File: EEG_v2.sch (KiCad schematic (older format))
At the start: 1 part

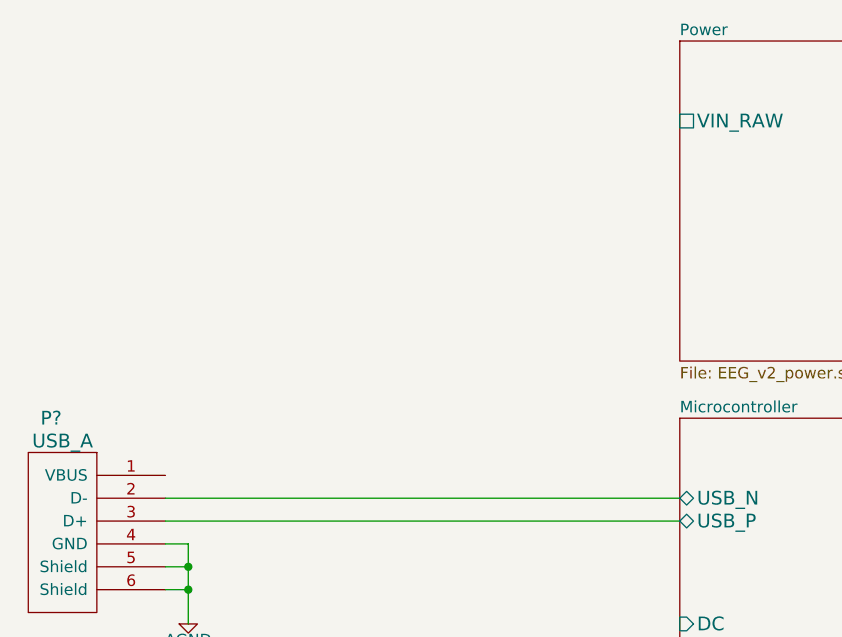
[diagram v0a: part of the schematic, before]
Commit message: Add battery connectors and switch
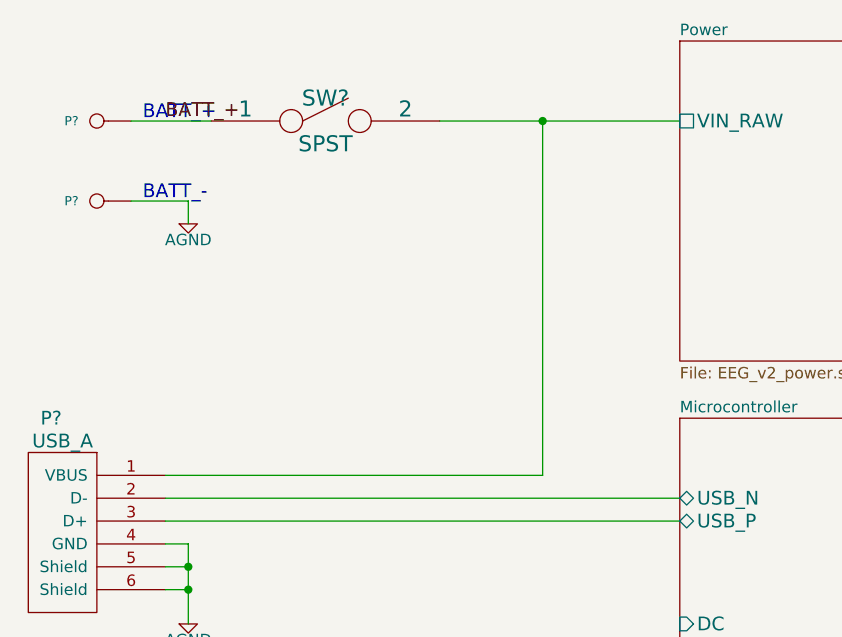
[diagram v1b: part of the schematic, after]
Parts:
- added P? (x2): CONN_1, ~, symbol CONN_1
- added SW?: SPST, ~, symbol SPST
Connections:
- net AGND: now also P?.1
- net Power/VIN_RAW: now also P?.1 (VBUS), SW?.2
- new net BATT_+: P?.1, SW?.1
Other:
- note added: "BATT_+"
- note added: "BATT_-"
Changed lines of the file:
@@
 	1    0    0    -1
 $EndComp
+$Comp
+L SPST SW?
+U 1 1 54C4411E
+P 3350 2900
+F 0 "SW?" H 3350 3000 70  0000 C CNN
+F 1 "SPST" H 3350 2800 70  0000 C CNN
+F 2 "~" H 3350 2900 60  0000 C CNN
+F 3 "~" H 3350 2900 60  0000 C CNN
+	1    3350 2900
+	1    0    0    -1
+$EndComp
+Wire Wire Line
+	3850 2900 4900 2900
+Wire Wire Line
+	2650 4450 4300 4450
+Wire Wire Line
+	4300 4450 4300 2900
+Connection ~ 4300 2900
+$Comp
+L CONN_1 P?
+U 1 1 54C44DCA
+P 2350 2900
+F 0 "P?" H 2430 2900 40  0000 L CNN
+F 1 "CONN_1" H 2350 2955 30  0001 C CNN
+F 2 "~" H 2350 2900 60  0000 C CNN
+F 3 "~" H 2350 2900 60  0000 C CNN
+	1    2350 2900
+	-1   0    0    1
+$EndComp
+$Comp
+L CONN_1 P?
+U 1 1 54C44DD9
+P 2350 3250
+F 0 "P?" H 2430 3250 40  0000 L CNN
+F 1 "CONN_1" H 2350 3305 30  0001 C CNN
+F 2 "~" H 2350 3250 60  0000 C CNN
+F 3 "~" H 2350 3250 60  0000 C CNN
+	1    2350 3250
+	-1   0    0    1
+$EndComp
+Wire Wire Line
+	2500 2900 2850 2900
+Wire Wire Line
+	2500 3250 2750 3250
+Wire Wire Line
+	2750 3250 2750 3350
+$Comp
+L AGND #PWR?
+U 1 1 54C45735
+P 2750 3350
+F 0 "#PWR?" H 2750 3350 40  0001 C CNN
+F 1 "AGND" H 2750 3280 50  0000 C CNN
+F 2 "~" H 2750 3350 60  0000 C CNN
+F 3 "~" H 2750 3350 60  0000 C CNN
+	1    2750 3350
+	1    0    0    -1
+$EndComp
+Text Notes 2550 2900 0    60   ~ 0
+BATT_+
+Text Label 2650 2900 0    60   ~ 0
+BATT_+
+Text Notes 2550 3250 0    60   ~ 0
+BATT_-
 $EndSCHEMATC

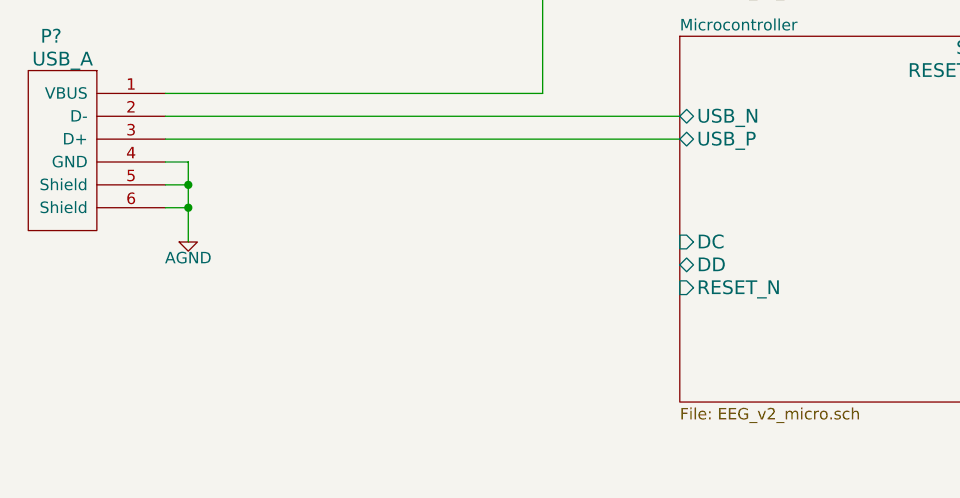
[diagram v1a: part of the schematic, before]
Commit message: Added debug / programming connector
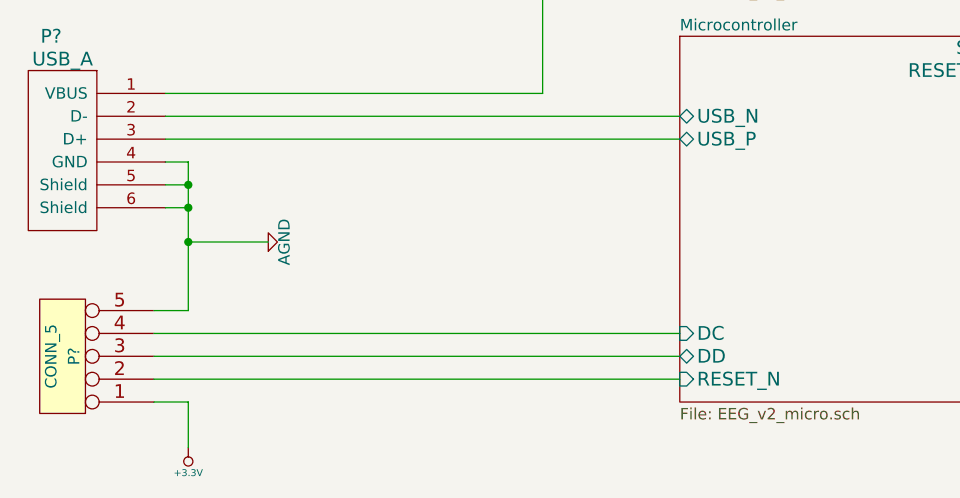
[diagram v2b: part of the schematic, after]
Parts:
- added P?: CONN_5, ~, symbol CONN_5
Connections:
- net AGND: now also P?.5
- net Microcontroller/DC: now also P?.4
- net Microcontroller/DD: now also P?.3
- net Microcontroller/RESET_N: now also P?.2
- new net +3.3V: P?.1
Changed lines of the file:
@@
 Sheet 1 4
 Title "Project Synapse Prototype Board"
-Date "23 jan 2015"
+Date "24 jan 2015"
 Rev "A.b"
 Comp "Senior Design 14-15"
@@
 F9 "USB_P" B L 4900 4650 60
 F10 "USB_N" B L 4900 4550 60
-F11 "RESET_N" I L 4900 5300 60
-F12 "DC" I L 4900 5100 60
-F13 "DD" B L 4900 5200 60
+F11 "RESET_N" I L 4900 5700 60
+F12 "DC" I L 4900 5500 60
+F13 "DD" B L 4900 5600 60
 $EndSheet
 $Comp
@@
 	2650 4750 2750 4750
 Wire Wire Line
-	2750 4750 2750 5100
+	2750 4750 2750 5400
 Wire Wire Line
 	2650 4850 2750 4850
@@
 L AGND #PWR?
 U 1 1 54C3BF39
-P 2750 5100
-F 0 "#PWR?" H 2750 5100 40  0001 C CNN
-F 1 "AGND" H 2750 5030 50  0000 C CNN
-F 2 "~" H 2750 5100 60  0000 C CNN
-F 3 "~" H 2750 5100 60  0000 C CNN
-	1    2750 5100
-	1    0    0    -1
+P 3100 5100
+F 0 "#PWR?" H 3100 5100 40  0001 C CNN
+F 1 "AGND" H 3100 5030 50  0000 C CNN
+F 2 "~" H 3100 5100 60  0000 C CNN
+F 3 "~" H 3100 5100 60  0000 C CNN
+	1    3100 5100
+	0    -1   -1   0
 $EndComp
 $Comp
@@
 Text Notes 2550 3250 0    60   ~ 0
 BATT_-
+$Comp
+L CONN_5 P?
+U 1 1 54C4DEF5
+P 2200 5600
+F 0 "P?" V 2150 5600 50  0000 C CNN
+F 1 "CONN_5" V 2250 5600 50  0000 C CNN
+F 2 "~" H 2200 5600 60  0000 C CNN
+F 3 "~" H 2200 5600 60  0000 C CNN
+	1    2200 5600
+	-1   0    0    1
+$EndComp
+Wire Wire Line
+	2750 5400 2600 5400
+Wire Wire Line
+	2750 5100 3100 5100
+Connection ~ 2750 5100
+Wire Wire Line
+	2600 5500 4900 5500
+Wire Wire Line
+	2600 5600 4900 5600
+Wire Wire Line
+	4900 5700 2600 5700
+Wire Wire Line
+	2600 5800 2750 5800
+Wire Wire Line
+	2750 5800 2750 6000
+$Comp
+L +3.3V #PWR?
+U 1 1 54C4F12C
+P 2750 6000
+F 0 "#PWR?" H 2750 5960 30  0001 C CNN
+F 1 "+3.3V" H 2750 6110 30  0000 C CNN
+F 2 "~" H 2750 6000 60  0000 C CNN
+F 3 "~" H 2750 6000 60  0000 C CNN
+	1    2750 6000
+	-1   0    0    1
+$EndComp
 $EndSCHEMATC

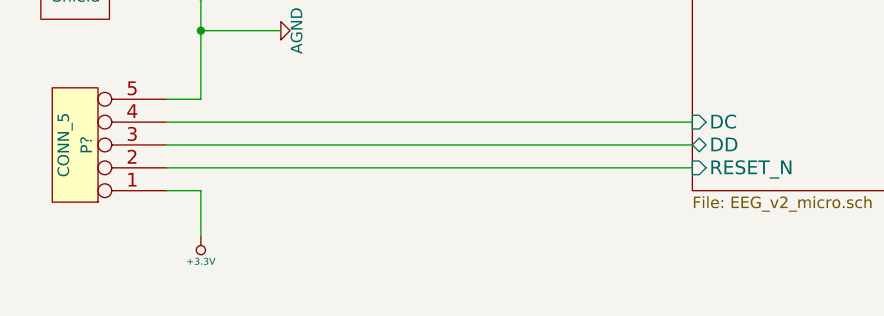
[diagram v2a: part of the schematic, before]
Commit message: Add note to debug connector for possible change.
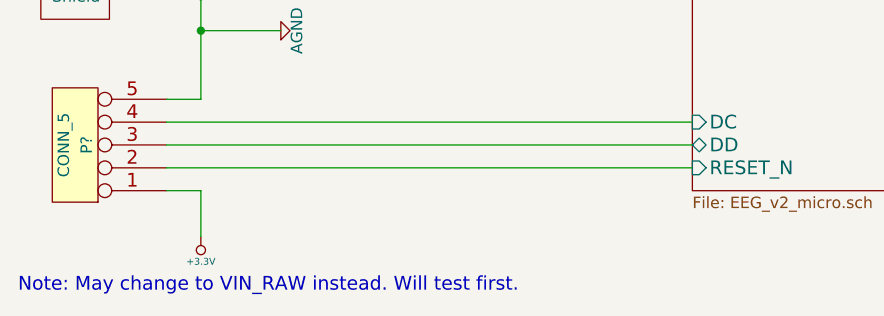
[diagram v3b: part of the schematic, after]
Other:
- note added: "Note: May change to VIN_RAW instead. Will test first."
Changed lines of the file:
@@
 	-1   0    0    1
 $EndComp
+Text Notes 1950 6250 0    60   ~ 0
+Note: May change to VIN_RAW instead. Will test first.
 $EndSCHEMATC

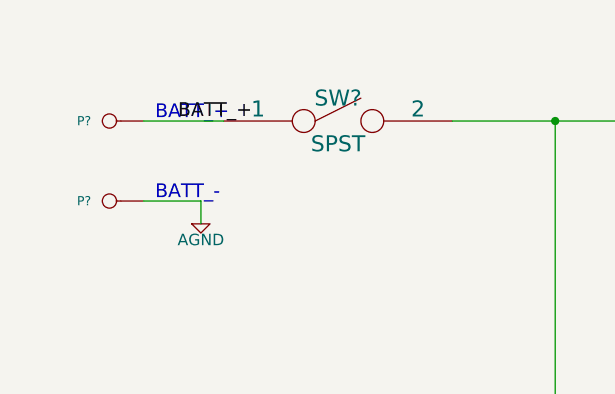
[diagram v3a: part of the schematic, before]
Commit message: Changed color of labels to be visible against bg.
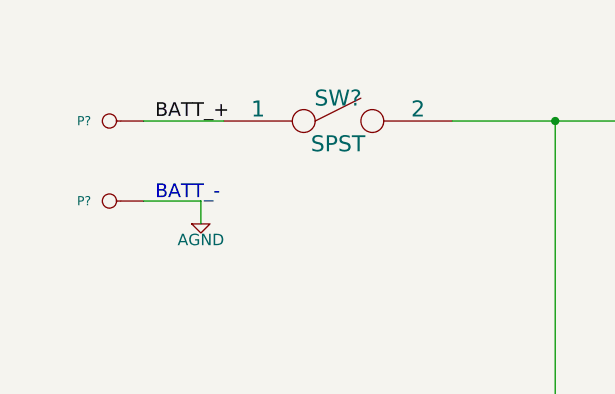
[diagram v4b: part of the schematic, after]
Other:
- note removed: "BATT_+"
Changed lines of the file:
@@
 	1    0    0    -1
 $EndComp
-Text Notes 2550 2900 0    60   ~ 0
-BATT_+
-Text Label 2650 2900 0    60   ~ 0
+Text Label 2550 2900 0    60   ~ 0
 BATT_+
 Text Notes 2550 3250 0    60   ~ 0

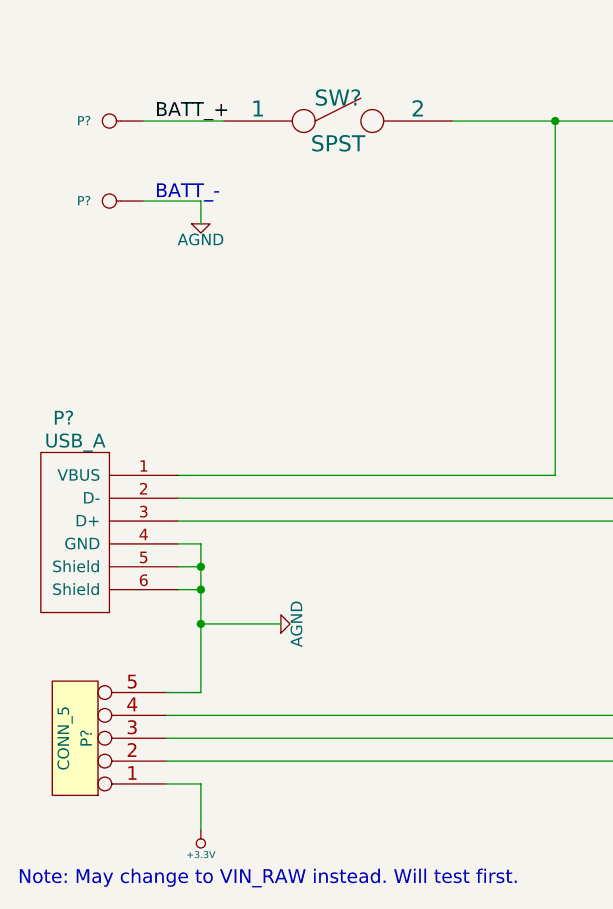
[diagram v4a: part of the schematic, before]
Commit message: Add symbol and footprints for SMD test points.
Add test points to power supplies.
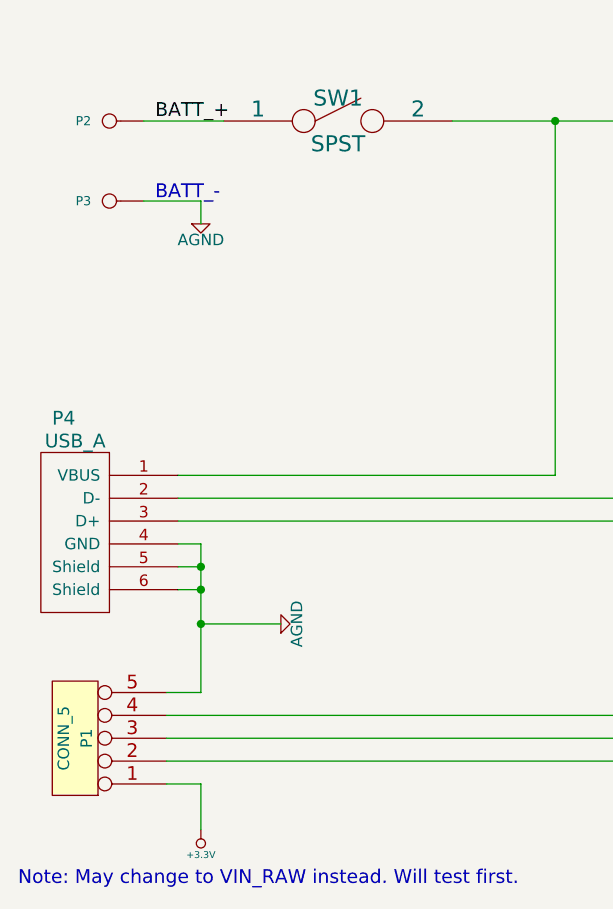
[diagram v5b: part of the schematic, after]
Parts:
- gave numbers to parts that had none: 5
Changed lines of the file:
@@
 $EndSheet
 $Comp
-L USB_A P?
+L USB_A P4
 U 1 1 54C36FB9
 P 2350 4700
-F 0 "P?" H 2150 5200 60  0000 C CNN
+F 0 "P4" H 2150 5200 60  0000 C CNN
 F 1 "USB_A" H 2200 5100 60  0000 C CNN
 F 2 "" H 1900 4700 60  0000 C CNN
@@
 Connection ~ 2750 4950
 $Comp
-L AGND #PWR?
+L AGND #PWR3
 U 1 1 54C3BF39
 P 3100 5100
-F 0 "#PWR?" H 3100 5100 40  0001 C CNN
+F 0 "#PWR3" H 3100 5100 40  0001 C CNN
 F 1 "AGND" H 3100 5030 50  0000 C CNN
 F 2 "~" H 3100 5100 60  0000 C CNN
@@
 $EndComp
 $Comp
-L SPST SW?
+L SPST SW1
 U 1 1 54C4411E
 P 3350 2900
-F 0 "SW?" H 3350 3000 70  0000 C CNN
+F 0 "SW1" H 3350 3000 70  0000 C CNN
 F 1 "SPST" H 3350 2800 70  0000 C CNN
 F 2 "~" H 3350 2900 60  0000 C CNN
@@
 Connection ~ 4300 2900
 $Comp
-L CONN_1 P?
+L CONN_1 P2
 U 1 1 54C44DCA
 P 2350 2900
-F 0 "P?" H 2430 2900 40  0000 L CNN
+F 0 "P2" H 2430 2900 40  0000 L CNN
 F 1 "CONN_1" H 2350 2955 30  0001 C CNN
 F 2 "~" H 2350 2900 60  0000 C CNN
@@
 $EndComp
 $Comp
-L CONN_1 P?
+L CONN_1 P3
 U 1 1 54C44DD9
 P 2350 3250
-F 0 "P?" H 2430 3250 40  0000 L CNN
+F 0 "P3" H 2430 3250 40  0000 L CNN
 F 1 "CONN_1" H 2350 3305 30  0001 C CNN
 F 2 "~" H 2350 3250 60  0000 C CNN
@@
 	2750 3250 2750 3350
 $Comp
-L AGND #PWR?
+L AGND #PWR1
 U 1 1 54C45735
 P 2750 3350
-F 0 "#PWR?" H 2750 3350 40  0001 C CNN
+F 0 "#PWR1" H 2750 3350 40  0001 C CNN
 F 1 "AGND" H 2750 3280 50  0000 C CNN
 F 2 "~" H 2750 3350 60  0000 C CNN
@@
 BATT_-
 $Comp
-L CONN_5 P?
+L CONN_5 P1
 U 1 1 54C4DEF5
 P 2200 5600
-F 0 "P?" V 2150 5600 50  0000 C CNN
+F 0 "P1" V 2150 5600 50  0000 C CNN
 F 1 "CONN_5" V 2250 5600 50  0000 C CNN
 F 2 "~" H 2200 5600 60  0000 C CNN
@@
 	2750 5800 2750 6000
 $Comp
-L +3.3V #PWR?
+L +3.3V #PWR2
 U 1 1 54C4F12C
 P 2750 6000
-F 0 "#PWR?" H 2750 5960 30  0001 C CNN
+F 0 "#PWR2" H 2750 5960 30  0001 C CNN
 F 1 "+3.3V" H 2750 6110 30  0000 C CNN
 F 2 "~" H 2750 6000 60  0000 C CNN

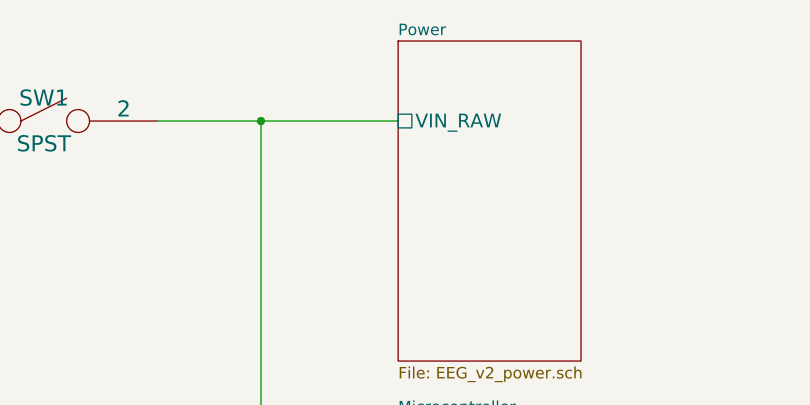
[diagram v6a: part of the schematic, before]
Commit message: Clean ERC errors.
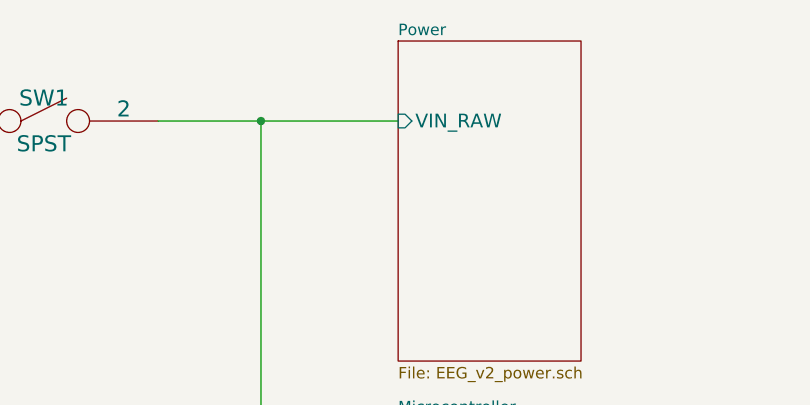
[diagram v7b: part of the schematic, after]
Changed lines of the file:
@@
 F0 "Power" 50
 F1 "EEG_v2_power.sch" 50
-F2 "VIN_RAW" U L 4900 2900 60
+F2 "VIN_RAW" I L 4900 2900 60
 $EndSheet
 $Sheet
